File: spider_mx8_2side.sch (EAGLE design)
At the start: 6 parts, among them J1 AVR_SPI_PRG_6NS

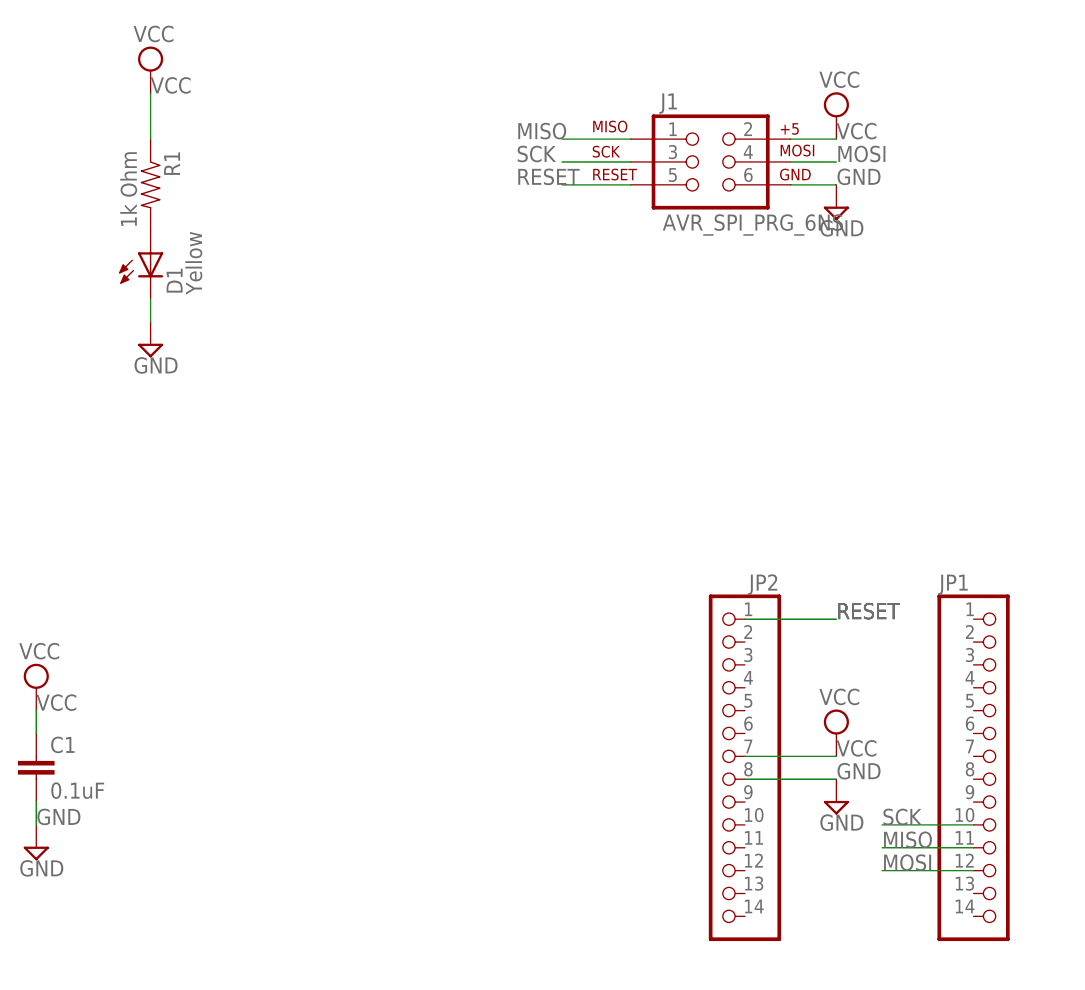
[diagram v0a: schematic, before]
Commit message: untested, but probably good 2sided board
using thin pins.  need to check DRC for whatever foundry use
(esp the edge-routing may give trouble)
(also, the label layer on the bottom side.  think gold phoenix doesn't
do that.)
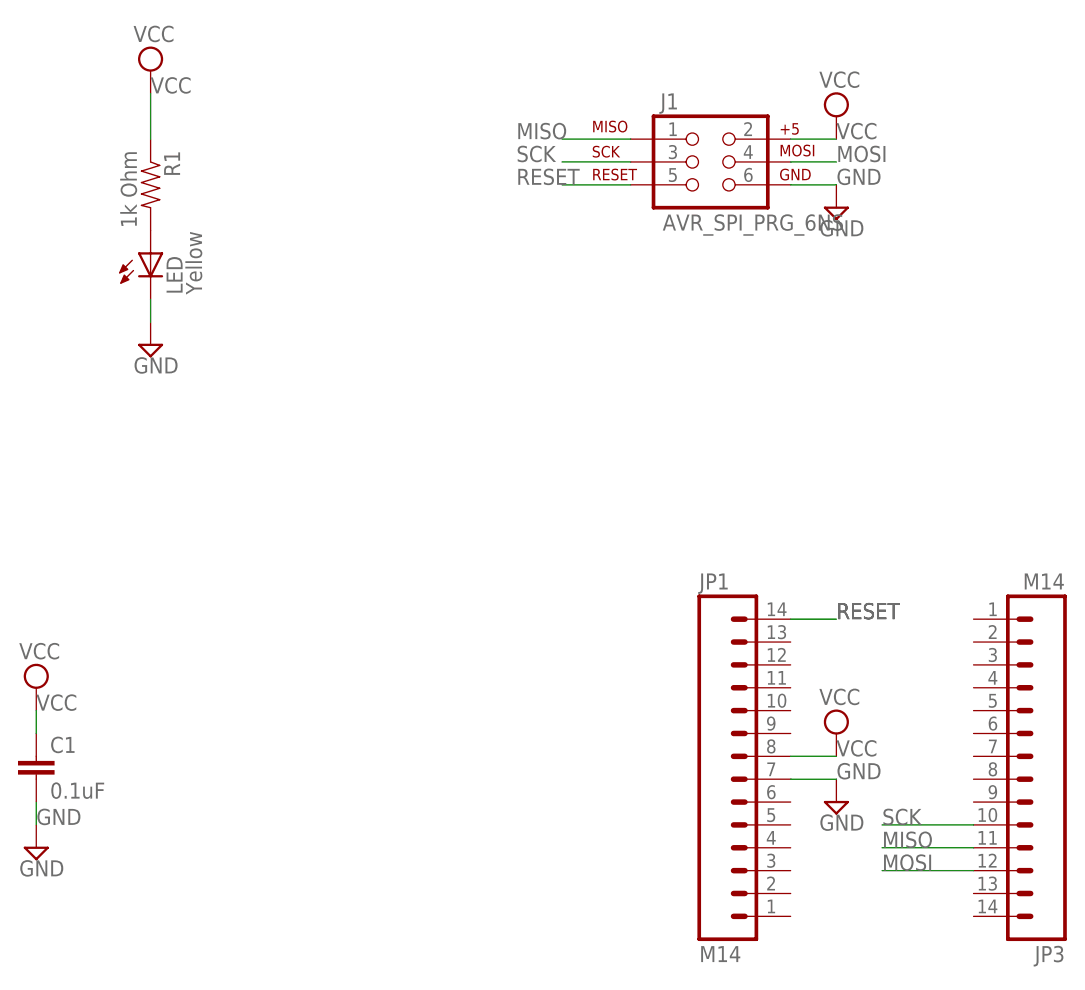
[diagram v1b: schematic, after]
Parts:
- removed JP2: (no value), pinhead:PINHD-1X14
- added JP3: M14, SparkFun-Connectors:M14
- JP1: value (none) -> M14; device pinhead:PINHD-1X14 -> SparkFun-Connectors:M14
- renumbered D1 to LED
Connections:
- net GND: now also JP1.7; no longer JP2.8
- net MISO: now also JP3.11; no longer JP1.11
- net MOSI: now also JP3.12; no longer JP1.12
- net RESET: now also JP1.14; no longer JP2.1
- net SCK: now also JP3.10; no longer JP1.10
- net VCC: now also JP1.8; no longer JP2.7
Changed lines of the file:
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@@
 <parts>
 <part name="J1" library="SparkFun-Connectors" deviceset="AVR_SPI_PRG_6" device="NS"/>
-<part name="JP1" library="pinhead" deviceset="PINHD-1X14" device=""/>
-<part name="JP2" library="pinhead" deviceset="PINHD-1X14" device=""/>
 <part name="R1" library="SparkFun-Passives" deviceset="RESISTOR" device="1206" value="1k Ohm"/>
-<part name="D1" library="SparkFun-LED" deviceset="LED-YELLOW" device="LILYPAD" value="Yellow"/>
+<part name="LED" library="SparkFun-LED" deviceset="LED-YELLOW" device="LILYPAD" value="Yellow"/>
 <part name="SUPPLY5" library="supply2" deviceset="GND" device=""/>
 <part name="C1" library="SparkFun-Passives" deviceset="CAP" device="1206" value="0.1uF"/>
@@
 <part name="SUPPLY9" library="supply2" deviceset="GND" device=""/>
 <part name="SUPPLY10" library="supply2" deviceset="GND" device=""/>
+<part name="JP3" library="SparkFun-Connectors" deviceset="M14" device=""/>
+<part name="JP1" library="SparkFun-Connectors" deviceset="M14" device=""/>
 </parts>
 <sheets>
@@
 <instances>
 <instance part="J1" gate="G$1" x="53.34" y="63.5"/>
-<instance part="JP1" gate="A" x="86.36" y="-2.54"/>
-<instance part="JP2" gate="A" x="55.88" y="-2.54" rot="MR0"/>
 <instance part="R1" gate="G$1" x="-7.62" y="60.96" rot="R270"/>
-<instance part="D1" gate="G$1" x="-7.62" y="53.34"/>
+<instance part="LED" gate="G$1" x="-7.62" y="53.34"/>
 <instance part="SUPPLY5" gate="GND" x="-7.62" y="43.18"/>
 <instance part="C1" gate="G$1" x="-20.32" y="-5.08"/>
@@
 <instance part="SUPPLY9" gate="GND" x="68.58" y="-7.62"/>
 <instance part="SUPPLY10" gate="GND" x="-20.32" y="-12.7"/>
+<instance part="JP3" gate="G$1" x="93.98" y="-5.08" rot="R180"/>
+<instance part="JP1" gate="G$1" x="53.34" y="-2.54"/>
 </instances>
 <busses>
@@
 </segment>
 <segment>
-<pinref part="JP1" gate="A" pin="10"/>
 <wire x1="83.82" y1="-10.16" x2="73.66" y2="-10.16" width="0.1524" layer="91"/>
 <label x="73.66" y="-10.16" size="1.778" layer="95"/>
+<pinref part="JP3" gate="G$1" pin="10"/>
 </segment>
 </net>
@@
 </segment>
 <segment>
-<pinref part="JP1" gate="A" pin="11"/>
 <wire x1="83.82" y1="-12.7" x2="73.66" y2="-12.7" width="0.1524" layer="91"/>
 <label x="73.66" y="-12.7" size="1.778" layer="95"/>
+<pinref part="JP3" gate="G$1" pin="11"/>
 </segment>
 </net>
@@
 </segment>
 <segment>
-<pinref part="JP1" gate="A" pin="12"/>
 <wire x1="83.82" y1="-15.24" x2="73.66" y2="-15.24" width="0.1524" layer="91"/>
 <label x="73.66" y="-15.24" size="1.778" layer="95"/>
+<pinref part="JP3" gate="G$1" pin="12"/>
 </segment>
 </net>
@@
 </segment>
 <segment>
-<pinref part="JP2" gate="A" pin="1"/>
-<wire x1="58.42" y1="12.7" x2="68.58" y2="12.7" width="0.1524" layer="91"/>
+<wire x1="63.5" y1="12.7" x2="68.58" y2="12.7" width="0.1524" layer="91"/>
 <label x="68.58" y="12.7" size="1.778" layer="95"/>
 <label x="68.58" y="12.7" size="1.778" layer="95"/>
+<pinref part="JP1" gate="G$1" pin="14"/>
 </segment>
 </net>
@@
 </segment>
 <segment>
-<pinref part="JP2" gate="A" pin="7"/>
-<wire x1="58.42" y1="-2.54" x2="68.58" y2="-2.54" width="0.1524" layer="91"/>
+<wire x1="63.5" y1="-2.54" x2="68.58" y2="-2.54" width="0.1524" layer="91"/>
 <label x="68.58" y="-2.54" size="1.778" layer="95"/>
 <pinref part="SUPPLY6" gate="G$1" pin="VCC"/>
+<pinref part="JP1" gate="G$1" pin="8"/>
 </segment>
 <segment>
@@
 </segment>
 <segment>
-<pinref part="JP2" gate="A" pin="8"/>
-<wire x1="58.42" y1="-5.08" x2="68.58" y2="-5.08" width="0.1524" layer="91"/>
+<wire x1="63.5" y1="-5.08" x2="68.58" y2="-5.08" width="0.1524" layer="91"/>
 <label x="68.58" y="-5.08" size="1.778" layer="95"/>
 <pinref part="SUPPLY9" gate="GND" pin="GND"/>
+<pinref part="JP1" gate="G$1" pin="7"/>
 </segment>
 <segment>
-<pinref part="D1" gate="G$1" pin="C"/>
+<pinref part="LED" gate="G$1" pin="C"/>
 <pinref part="SUPPLY5" gate="GND" pin="GND"/>
 <wire x1="-7.62" y1="48.26" x2="-7.62" y2="45.72" width="0.1524" layer="91"/>
@@
 <segment>
 <pinref part="R1" gate="G$1" pin="2"/>
-<pinref part="D1" gate="G$1" pin="A"/>
+<pinref part="LED" gate="G$1" pin="A"/>
 </segment>
 </net>
